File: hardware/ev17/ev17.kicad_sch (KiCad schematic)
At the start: 183 parts, among them CN1 Conn_05x02_Female, CN2 PJ-242, J1 USB_C_Receptacle, J10 Conn_02x05_Counter_Clockwise, J11 Conn_02x05_Counter_Clockwise, J17 Conn_01x01, J18 Conn_01x01, J19 Conn_01x01, J2 Conn_01x02_Socket, J3 AudioJack4, J4 Conn_02x03_Odd_Even, J5 Conn_02x03_Odd_Even, J6 Conn_02x05_Counter_Clockwise, J7 Conn_02x05_Counter_Clockwise, J8 Conn_02x05_Counter_Clockwise, J9 Conn_02x05_Counter_Clockwise, Q1 2N7002, Q2 2N7002, Q3 2N7002, SW1 SW_SPDT, SW2 SW_Push, SW3 SW_Push, SW4 SW_Push, SW5 SW_Push, SW6 SW_Push, SW7 SW_Push, U1 BQ21040DBV, U10 STM32F405RGTx, U12 XC6227C301MR-G, U2 USBLC6-2P6, U3 STM32F072CBTx, U4 CH340C, U5 TPS63060, U6 WM8960CGEFL/RV, U7 ESP32-S3-WROOM-1, U8 M24C02-RMN6TP, U9 TPS2116DRL, Y1 Crystal_GND24

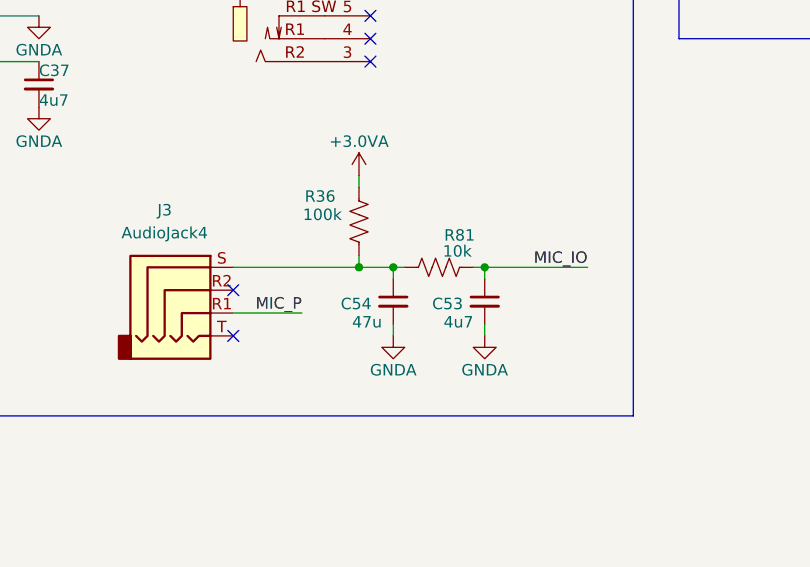
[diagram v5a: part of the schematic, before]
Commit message: updated the capacitor values for the mic io line. (refs #408)
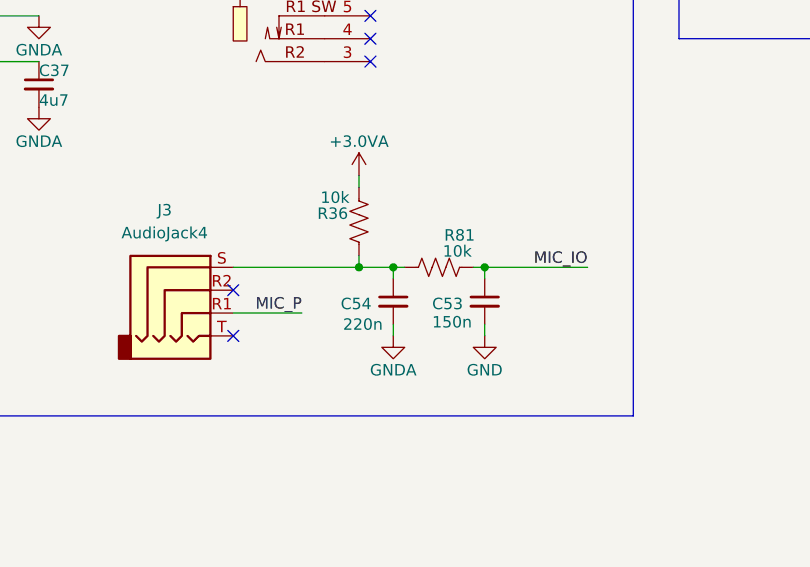
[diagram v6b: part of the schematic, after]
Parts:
- C53: value 4u7 -> 150n; JLCPCB Part # C23733 -> C505466
- C54: value 47u -> 220n; footprint Capacitor_SMD:C_0805_2012Metric -> Capacitor_SMD:C_0402_1005Metric; JLCPCB Part # C16780 -> C16772
- R36: value 100k -> 10k; JLCPCB Part # C25741 -> C25744
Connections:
- net GND: now also C53.2
- net GNDA: no longer C53.2
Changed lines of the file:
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@@
 			)
 		)
-		(property "Value" "4u7"
-			(at 351.028 247.396 0)
+		(property "Value" "150n"
+			(at 349.758 247.396 0)
 			(effects
 				(font
@@
 			)
 		)
-		(property "JLCPCB Part #" "C23733"
+		(property "JLCPCB Part #" "C505466"
 			(at 355.6 245.11 0)
 			(effects
@@
 	)
 	(symbol
-		(lib_id "Device:R_US")
-		(at 341.63 236.22 180)
-		(unit 1)
-		(exclude_from_sim no)
-		(in_bom yes)
-		(on_board yes)
-		(dnp no)
-		(property "Reference" "R36"
-			(at 337.312 233.426 0)
-			(effects
-				(font
-					(size 1.27 1.27)
-				)
-			)
-		)
-		(property "Value" "100k"
-			(at 337.566 235.458 0)
-			(effects
-				(font
-					(size 1.27 1.27)
-				)
-			)
-		)
-		(property "Footprint" "Resistor_SMD:R_0402_1005Metric"
-			(at 343.408 236.22 90)
-			(effects
-				(font
-					(size 1.27 1.27)
-				)
-				(hide yes)
-			)
-		)
-		(property "Datasheet" "~"
-			(at 341.63 236.22 0)
-			(effects
-				(font
-					(size 1.27 1.27)
-				)
-				(hide yes)
-			)
-		)
-		(property "Description" "Resistor, US symbol"
-			(at 341.63 236.22 0)
-			(effects
-				(font
-					(size 1.27 1.27)
-				)
-				(hide yes)
-			)
-		)
-		(property "JLCPCB Part #" "C25741"
-			(at 341.63 236.22 0)
-			(effects
-				(font
-					(size 1.27 1.27)
-				)
-				(hide yes)
-			)
-		)
-		(property "Availability" ""
-			(at 341.63 236.22 0)
-			(effects
-				(font
-					(size 1.27 1.27)
-				)
-			)
-		)
-		(property "Sim.Device" ""
-			(at 341.63 236.22 0)
-			(effects
-				(font
-					(size 1.27 1.27)
-				)
-			)
-		)
-		(property "JLCPCB Position Offset" ""
-			(at 341.63 236.22 0)
-			(effects
-				(font
-					(size 1.27 1.27)
-				)
-				(hide yes)
-			)
-		)
-		(property "Sim.Type" ""
-			(at 341.63 236.22 0)
-			(effects
-				(font
-					(size 1.27 1.27)
-				)
-				(hide yes)
-			)
-		)
-		(pin "1"
-		)
-		(pin "2"
-		)
-		(instances
-			(project "ev17"
-				(path "/bd865368-262b-4f76-b7a6-1673c2cb0f8c"
-					(reference "R36")
-					(unit 1)
-				)
-			)
-		)
-	)
-	(symbol
 		(lib_id "Device:R_Small_US")
 		(at 101.6 325.12 180)
@@
 	(symbol
 		(lib_id "Device:R_US")
+		(at 341.63 236.22 180)
+		(unit 1)
+		(exclude_from_sim no)
+		(in_bom yes)
+		(on_board yes)
+		(dnp no)
+		(property "Reference" "R36"
+			(at 338.709 235.331 0)
+			(effects
+				(font
+					(size 1.27 1.27)
+				)
+			)
+		)
+		(property "Value" "10k"
+			(at 338.963 233.553 0)
+			(effects
+				(font
+					(size 1.27 1.27)
+				)
+			)
+		)
+		(property "Footprint" "Resistor_SMD:R_0402_1005Metric"
+			(at 343.408 236.22 90)
+			(effects
+				(font
+					(size 1.27 1.27)
+				)
+				(hide yes)
+			)
+		)
+		(property "Datasheet" "~"
+			(at 341.63 236.22 0)
+			(effects
+				(font
+					(size 1.27 1.27)
+				)
+				(hide yes)
+			)
+		)
+		(property "Description" "Resistor, US symbol"
+			(at 341.63 236.22 0)
+			(effects
+				(font
+					(size 1.27 1.27)
+				)
+				(hide yes)
+			)
+		)
+		(property "JLCPCB Part #" "C25744"
+			(at 341.63 236.22 0)
+			(effects
+				(font
+					(size 1.27 1.27)
+				)
+				(hide yes)
+			)
+		)
+		(property "Availability" ""
+			(at 341.63 236.22 0)
+			(effects
+				(font
+					(size 1.27 1.27)
+				)
+			)
+		)
+		(property "Sim.Device" ""
+			(at 341.63 236.22 0)
+			(effects
+				(font
+					(size 1.27 1.27)
+				)
+			)
+		)
+		(property "JLCPCB Position Offset" ""
+			(at 341.63 236.22 0)
+			(effects
+				(font
+					(size 1.27 1.27)
+				)
+				(hide yes)
+			)
+		)
+		(property "Sim.Type" ""
+			(at 341.63 236.22 0)
+			(effects
+				(font
+					(size 1.27 1.27)
+				)
+				(hide yes)
+			)
+		)
+		(pin "1"
+		)
+		(pin "2"
+		)
+		(instances
+			(project "ev17"
+				(path "/bd865368-262b-4f76-b7a6-1673c2cb0f8c"
+					(reference "R36")
+					(unit 1)
+				)
+			)
+		)
+	)
+	(symbol
+		(lib_id "Device:R_US")
 		(at 515.62 227.33 0)
 		(unit 1)
@@
 			)
 		)
-		(property "Value" "47u"
-			(at 340.868 247.396 0)
+		(property "Value" "220n"
+			(at 339.852 247.65 0)
 			(effects
 				(font
@@
 			)
 		)
-		(property "Footprint" "Capacitor_SMD:C_0805_2012Metric"
+		(property "Footprint" "Capacitor_SMD:C_0402_1005Metric"
 			(at 345.44 245.11 0)
 			(effects
@@
 			)
 		)
-		(property "JLCPCB Part #" "C16780"
+		(property "JLCPCB Part #" "C16772"
 			(at 345.44 245.11 0)
 			(effects
@@
 	)
 	(symbol
+		(lib_id "power:GND")
+		(at 355.6 248.92 0)
+		(unit 1)
+		(exclude_from_sim no)
+		(in_bom yes)
+		(on_board yes)
+		(dnp no)
+		(property "Reference" "#PWR090"
+			(at 355.6 255.27 0)
+			(effects
+				(font
+					(size 1.27 1.27)
+				)
+				(hide yes)
+			)
+		)
+		(property "Value" "GND"
+			(at 355.6 252.73 0)
+			(effects
+				(font
+					(size 1.27 1.27)
+				)
+			)
+		)
+		(property "Footprint" ""
+			(at 355.6 248.92 0)
+			(effects
+				(font
+					(size 1.27 1.27)
+				)
+				(hide yes)
+			)
+		)
+		(property "Datasheet" ""
+			(at 355.6 248.92 0)
+			(effects
+				(font
+					(size 1.27 1.27)
+				)
+				(hide yes)
+			)
+		)
+		(property "Description" "Power symbol creates a global label with name \"GND\" , ground"
+			(at 355.6 248.92 0)
+			(effects
+				(font
+					(size 1.27 1.27)
+				)
+				(hide yes)
+			)
+		)
+		(pin "1"
+		)
+		(instances
+			(project "ev17"
+				(path "/bd865368-262b-4f76-b7a6-1673c2cb0f8c"
+					(reference "#PWR090")
+					(unit 1)
+				)
+			)
+		)
+	)
+	(symbol
 		(lib_id "Device:C_Small")
 		(at 306.07 220.98 0)
@@
 					(unit 1)
 				)
-			)
-		)
-	)
-	(symbol
-		(lib_id "power:GNDA")
-		(at 355.6 248.92 0)
-		(unit 1)
-		(exclude_from_sim no)
-		(in_bom yes)
-		(on_board yes)
-		(dnp no)
-		(property "Reference" "#PWR090"
-			(at 355.6 255.27 0)
-			(effects
-				(font
-					(size 1.27 1.27)
-				)
-				(hide yes)
-			)
-		)
-		(property "Value" "GNDA"
-			(at 355.6 252.73 0)
-			(effects
-				(font
-					(size 1.27 1.27)
-				)
-			)
-		)
-		(property "Footprint" ""
-			(at 355.6 248.92 0)
-			(effects
-				(font
-					(size 1.27 1.27)
-				)
-				(hide yes)
-			)
-		)
-		(property "Datasheet" ""
-			(at 355.6 248.92 0)
-			(effects
-				(font
-					(size 1.27 1.27)
-				)
-				(hide yes)
-			)
-		)
-		(property "Description" "Power symbol creates a global label with name \"GNDA\" , analog ground"
-			(at 355.6 248.92 0)
-			(effects
-				(font
-					(size 1.27 1.27)
-				)
-				(hide yes)
-			)
-		)
-		(pin "1"
-		)
-		(instances
-			(project "ev17"
-				(path "/bd865368-262b-4f76-b7a6-1673c2cb0f8c"
-					(reference "#PWR090")
-					(unit 1)
-				)

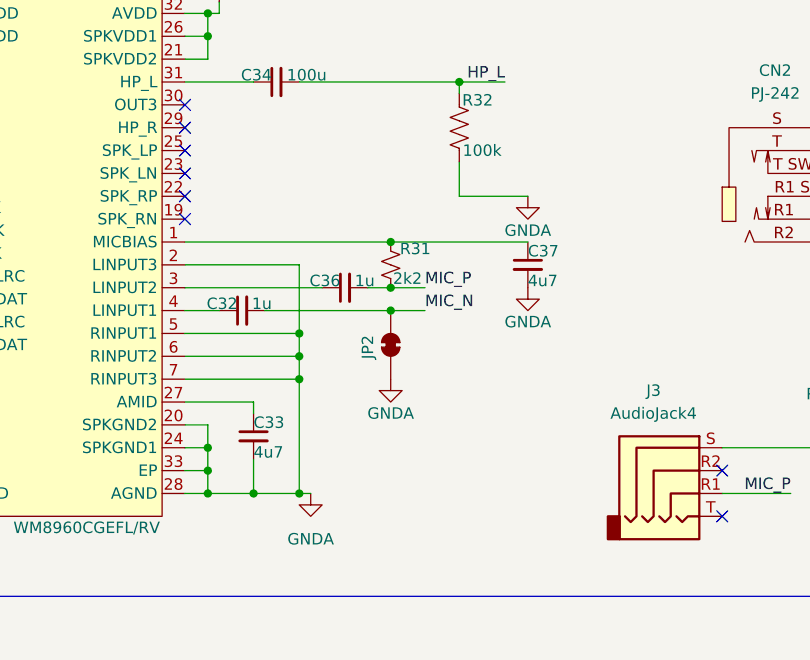
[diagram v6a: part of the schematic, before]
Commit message: Added 100nF caps to amid and micbias (refs #412)
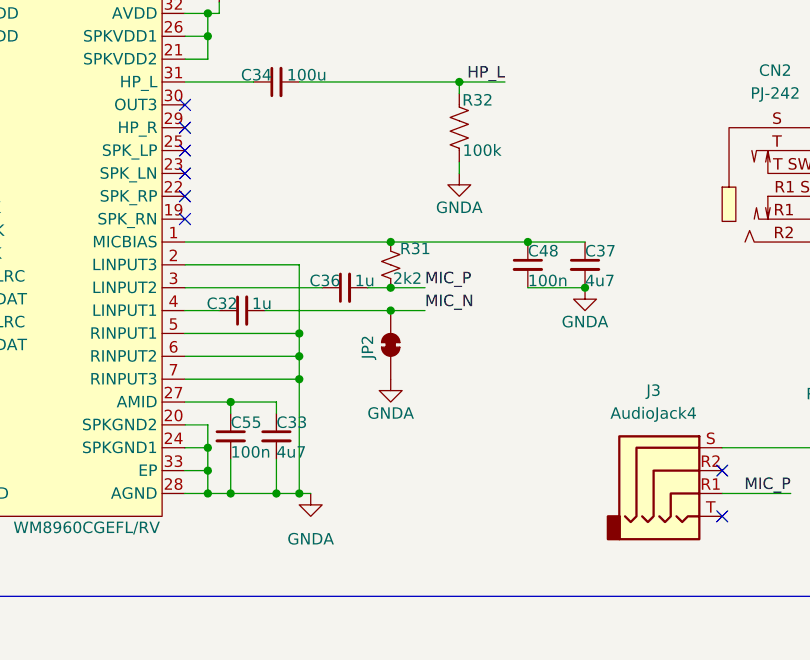
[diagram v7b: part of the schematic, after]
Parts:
- added C48, C55: 100n, Capacitor_SMD:C_0402_1005Metric, symbol Device:C_Small
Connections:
- net GNDA: now also C48.2, C55.2
- net at C37.1, R31.2, U6.1 (MICBIAS): now also C48.1
- net at C33.1, U6.27 (AMID): now also C55.1
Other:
- moved on the sheet: C33, C37
